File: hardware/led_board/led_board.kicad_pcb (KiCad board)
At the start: 2 copper layers, 63.5 x 45.7 mm, 22 parts, among them P1 CONN_01X03, P2 CONN_01X03, P3 CONN_01X01, P4 CONN_01X01, P5 CONN_01X01, P6 CONN_01X01

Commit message: Cleaned up for git import
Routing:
- net Net-(D12-Pad1): track 123.9 -> 122.9 mm
- net Net-(D3-Pad1): track 83.1 -> 82.5 mm
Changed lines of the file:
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@@
     (thickness 1.6)
     (drawings 14)
-    (tracks 52)
+    (tracks 54)
     (zones 0)
     (modules 22)
@@
   (segment (start 160.528 94.742) (end 142.24 94.742) (width 0.889) (layer F.Cu) (net 2))
   (segment (start 180.848 94.742) (end 162.56 94.742) (width 0.889) (layer F.Cu) (net 3))
+  (segment (start 139.7 109.22) (end 135.255 109.22) (width 1.905) (layer F.Cu) (net 4))
+  (segment (start 182.88 109.855) (end 180.975 111.76) (width 1.905) (layer F.Cu) (net 4))
+  (segment (start 180.975 111.76) (end 142.24 111.76) (width 1.905) (layer F.Cu) (net 4))
+  (segment (start 142.24 111.76) (end 139.7 109.22) (width 1.905) (layer F.Cu) (net 4))
   (segment (start 182.88 104.902) (end 182.88 109.855) (width 1.905) (layer F.Cu) (net 4))
-  (segment (start 133.604002 102.615998) (end 134.62 101.6) (width 1.905) (layer F.Cu) (net 4))
-  (segment (start 133.604002 107.95) (end 133.604002 102.615998) (width 1.905) (layer F.Cu) (net 4))
-  (segment (start 134.874002 109.22) (end 133.604002 107.95) (width 1.905) (layer F.Cu) (net 4))
-  (segment (start 139.7 109.22) (end 134.874002 109.22) (width 1.905) (layer F.Cu) (net 4))
-  (segment (start 142.24 111.76) (end 139.7 109.22) (width 1.905) (layer F.Cu) (net 4))
-  (segment (start 180.975 111.76) (end 142.24 111.76) (width 1.905) (layer F.Cu) (net 4))
-  (segment (start 182.88 109.855) (end 180.975 111.76) (width 1.905) (layer F.Cu) (net 4))
+  (segment (start 133.985 107.95) (end 133.985 102.235) (width 1.905) (layer F.Cu) (net 4))
+  (segment (start 135.255 109.22) (end 133.985 107.95) (width 1.905) (layer F.Cu) (net 4))
+  (segment (start 133.985 102.235) (end 134.62 101.6) (width 1.905) (layer F.Cu) (net 4))
   (segment (start 189.738 101.6) (end 186.69 101.6) (width 1.905) (layer F.Cu) (net 4))
   (segment (start 182.88 97.79) (end 182.88 94.742) (width 1.905) (layer F.Cu) (net 4))
@@
   (segment (start 189.738 101.6) (end 186.182 101.6) (width 1.905) (layer F.Cu) (net 4))
   (segment (start 186.182 101.6) (end 182.88 104.902) (width 1.905) (layer F.Cu) (net 4))
-  (segment (start 140.208 104.902) (end 140.208 102.362) (width 0.889) (layer F.Cu) (net 5) (status 400000))
-  (segment (start 140.97 101.6) (end 145.49 101.6) (width 0.889) (layer F.Cu) (net 5) (status 800000))
+  (segment (start 140.208 104.902) (end 140.208 102.362) (width 0.889) (layer F.Cu) (net 5))
+  (segment (start 140.97 101.6) (end 145.49 101.6) (width 0.889) (layer F.Cu) (net 5))
   (segment (start 140.208 102.362) (end 140.97 101.6) (width 0.889) (layer F.Cu) (net 5))
   (segment (start 160.528 104.902) (end 142.24 104.902) (width 0.889) (layer F.Cu) (net 6))
@@
   (segment (start 142.24 84.582) (end 160.528 84.582) (width 0.889) (layer F.Cu) (net 9))
   (segment (start 162.56 84.582) (end 180.848 84.582) (width 0.889) (layer F.Cu) (net 10))
-  (segment (start 131.445 99.695) (end 131.445 111.125) (width 1.905) (layer F.Cu) (net 11))
-  (segment (start 131.445 99.695) (end 132.08 99.06) (width 1.905) (layer F.Cu) (net 11))
-  (segment (start 134.62 99.06) (end 132.08 99.06) (width 1.905) (layer F.Cu) (net 11))
-  (segment (start 180.975 120.015) (end 182.88 118.11) (width 1.905) (layer F.Cu) (net 11))
-  (segment (start 140.335 120.015) (end 180.975 120.015) (width 1.905) (layer F.Cu) (net 11))
-  (segment (start 131.445 111.125) (end 140.335 120.015) (width 1.905) (layer F.Cu) (net 11))
+  (segment (start 182.88 115.062) (end 182.88 118.11) (width 1.905) (layer F.Cu) (net 11) (status 400000))
+  (segment (start 140.335 119.761) (end 181.229 119.761) (width 1.905) (layer F.Cu) (net 11))
+  (segment (start 133.35 99.06) (end 131.572 100.838) (width 1.905) (layer F.Cu) (net 11))
+  (segment (start 131.572 100.838) (end 131.572 111.506) (width 1.905) (layer F.Cu) (net 11))
+  (segment (start 131.572 111.506) (end 134.874 114.808) (width 1.905) (layer F.Cu) (net 11))
+  (segment (start 134.874 114.808) (end 135.382 114.808) (width 1.905) (layer F.Cu) (net 11))
+  (segment (start 135.382 114.808) (end 140.335 119.761) (width 1.905) (layer F.Cu) (net 11))
+  (segment (start 133.35 99.06) (end 134.62 99.06) (width 1.905) (layer F.Cu) (net 11))
+  (segment (start 182.88 118.11) (end 181.229 119.761) (width 1.905) (layer F.Cu) (net 11))
   (segment (start 189.738 99.06) (end 191.77 99.06) (width 1.905) (layer F.Cu) (net 11))
   (segment (start 189.992 84.582) (end 182.88 84.582) (width 1.905) (layer F.Cu) (net 11))
@@
   (segment (start 192.405 98.425) (end 192.405 86.995) (width 1.905) (layer F.Cu) (net 11))
   (segment (start 191.77 99.06) (end 192.405 98.425) (width 1.905) (layer F.Cu) (net 11))
-  (segment (start 182.88 115.062) (end 182.88 118.11) (width 1.905) (layer F.Cu) (net 11))
   (segment (start 189.738 99.06) (end 191.135 99.06) (width 1.905) (layer F.Cu) (net 11))
   (segment (start 188.468 115.062) (end 182.88 115.062) (width 1.905) (layer F.Cu) (net 11))
@@
   (segment (start 192.405 100.33) (end 192.405 111.125) (width 1.905) (layer F.Cu) (net 11))
   (segment (start 191.135 99.06) (end 192.405 100.33) (width 1.905) (layer F.Cu) (net 11))
-  (segment (start 140.208 115.062) (end 139.902 115.062) (width 0.889) (layer F.Cu) (net 12) (status C00000))
-  (segment (start 139.902 115.062) (end 137.16 112.32) (width 0.889) (layer F.Cu) (net 12) (status C00000))
-  (segment (start 142.24 115.062) (end 160.528 115.062) (width 0.889) (layer F.Cu) (net 13) (status C00000))
-  (segment (start 162.56 115.062) (end 180.848 115.062) (width 0.889) (layer F.Cu) (net 14) (status C00000))
+  (segment (start 140.208 115.062) (end 139.902 115.062) (width 0.889) (layer F.Cu) (net 12))
+  (segment (start 139.902 115.062) (end 137.16 112.32) (width 0.889) (layer F.Cu) (net 12))
+  (segment (start 142.24 115.062) (end 160.528 115.062) (width 0.889) (layer F.Cu) (net 13))
+  (segment (start 162.56 115.062) (end 180.848 115.062) (width 0.889) (layer F.Cu) (net 14))
   (segment (start 134.672 96.468) (end 134.62 96.52) (width 1.905) (layer F.Cu) (net 15))
   (segment (start 134.874 96.266) (end 134.62 96.52) (width 1.905) (layer F.Cu) (net 15))

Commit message: Added fab files
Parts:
- moved D12 2.54 mm to (186.7, 116.8)
- moved D3 2.54 mm to (186.7, 96.5)
- moved D6 2.54 mm to (186.7, 106.7)
- moved D9 2.54 mm to (186.7, 86.4)
- moved D11 1.27 mm to (165.1, 116.8)
- moved D2 1.27 mm to (165.1, 96.5)
- moved D5 1.27 mm to (165.1, 106.7)
- moved D8 1.27 mm to (165.1, 86.4)
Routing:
- net Net-(D3-Pad1): track 82.5 -> 89.6 mm
- net Net-(D12-Pad1): track 122.9 -> 120.4 mm
- net Net-(D7-Pad1): track 18.3 -> 19.6 mm
- net Net-(D4-Pad1): track 18.3 -> 19.6 mm
- net Net-(D10-Pad1): track 18.3 -> 19.6 mm
- net Net-(D1-Pad1): track 18.3 -> 19.6 mm
- net Net-(D8-Pad1): track 18.3 -> 19.6 mm
- net Net-(D5-Pad1): track 18.3 -> 19.6 mm
- net Net-(D2-Pad1): track 18.3 -> 19.6 mm
- net Net-(D11-Pad1): track 18.3 -> 19.6 mm
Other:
- rule pad_to_mask_clearance: 0.2 -> 0.1016
- board text added: "UnnaturalLight (LED board) - Rev 1"

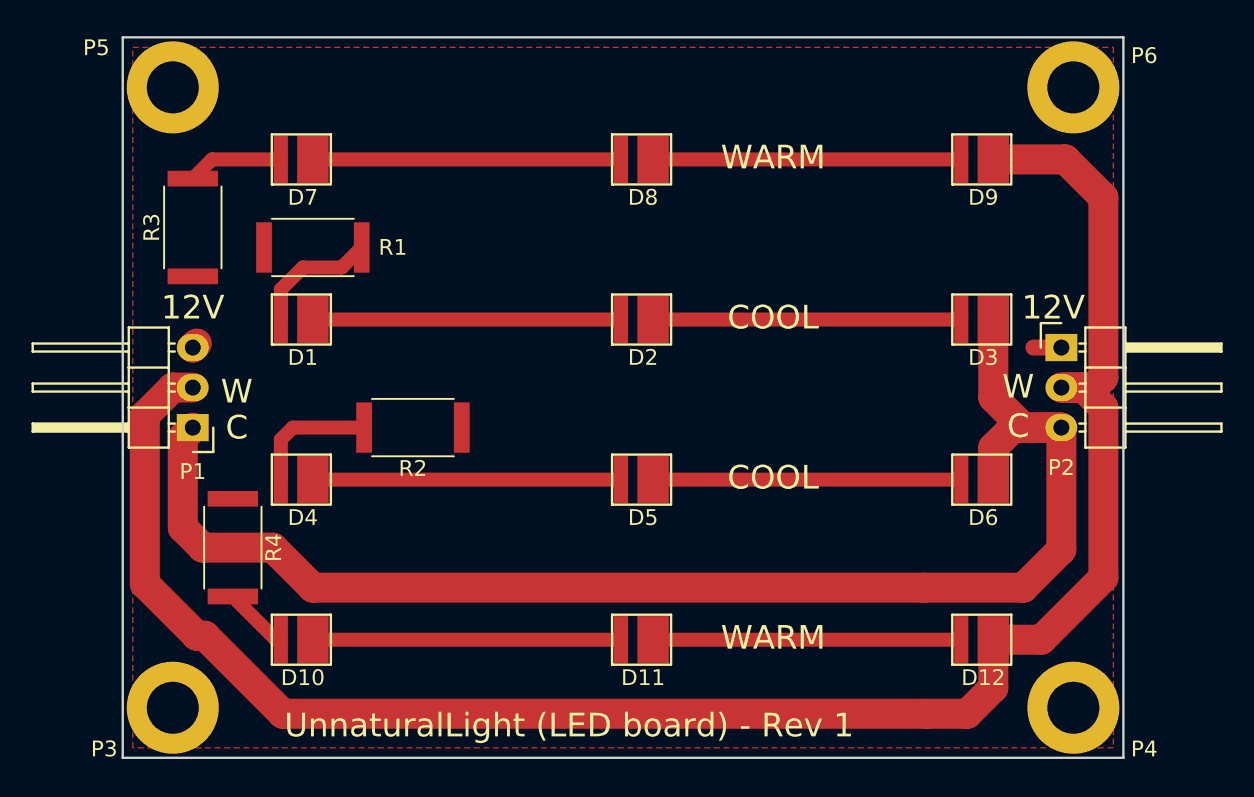
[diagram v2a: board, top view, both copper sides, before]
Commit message: Changed LED board connectors to SMD
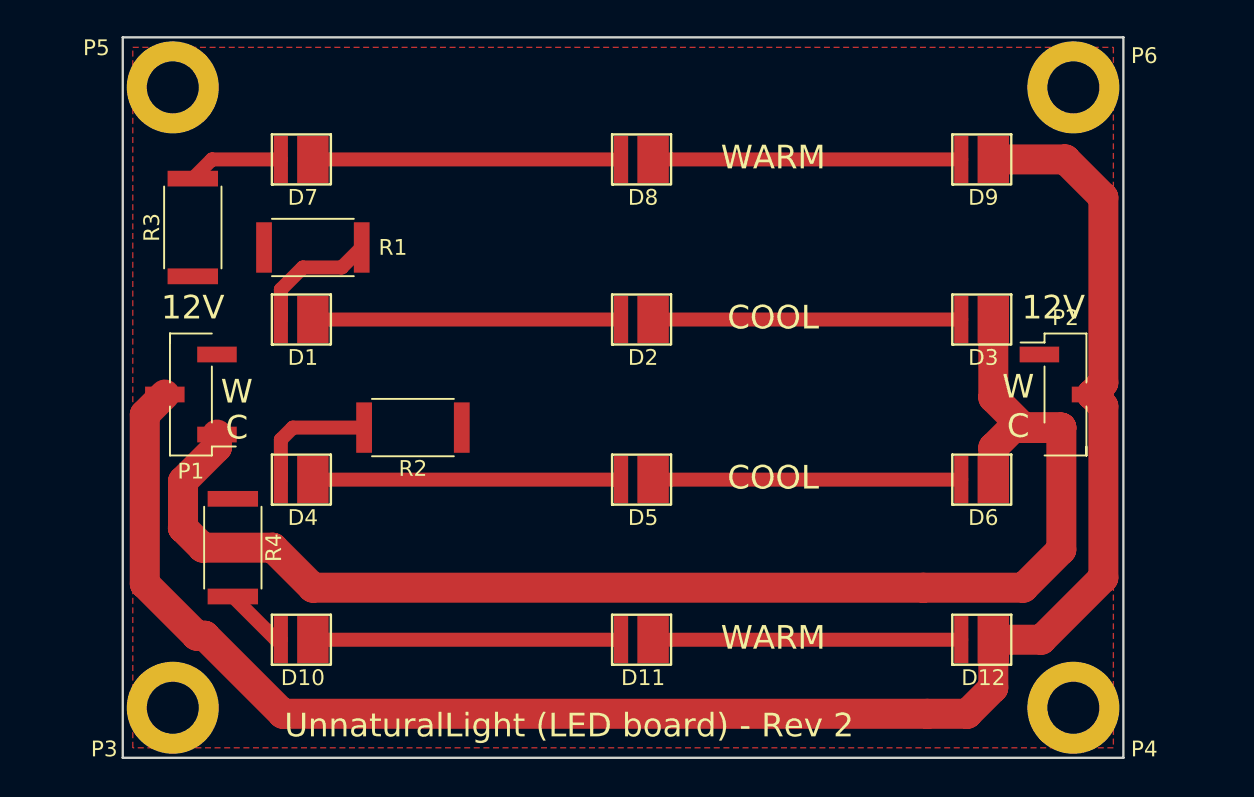
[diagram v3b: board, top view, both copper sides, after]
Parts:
- P1, P2: footprint Pin_Headers:Pin_Header_Angled_1x03 -> Pin_Headers:Pin_Header_Straight_1x03_Pitch2.54mm_SMD_Pin1Left
- moved P2 2.99 mm to (190.0, 99.5)
- moved P1 2.10 mm to (134.5, 99.5)
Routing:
- net Net-(D12-Pad1): track 120.4 -> 114.9 mm
- net +12V: track 1.45 -> 0.00 mm
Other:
- board text added: "UnnaturalLight (LED board) - Rev 2"
- board text removed: "UnnaturalLight (LED board) - Rev 1"
